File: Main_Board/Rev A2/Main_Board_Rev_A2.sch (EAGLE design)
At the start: 207 parts, among them J1 90814-0208, J12 22-27-2061-06, J15 1241050-5, J2 90814-0206, J3 90814-0208, J4 5504F1-09S-02A-03, J5 22-05-7048-04, J6 22-05-7048-04, J7 22-05-7058-05, J8 22-05-7048-04, K1 G6K-2G-Y, K2 G6K-2G-Y, K3 G6K-2G-Y, K4 G6K-2G-Y, P1 RB1-125BAG1A, SW1 B3FS-1015, SW2 B3FS-1015, T1 MMBT2222AL, U1 LT3686HDDPBF, U10 SN74LVC2G17DBVR, U11 MCP2561-E/SN, U12 TLV313, U2 TPL0401A, U3 SN74LVC3G17DCTR, U4 SN74LVC3G17DCTR, U5 LT3686HDDPBF, U6 LPC1768FBD100, U7 AT24C512C-SSHM-B, U8 SN74LVC3G17DCTR, U9 SN74LVC2G17DBVR, X1 ASE_50, X12 22-05-7028-02, X13 22-05-7028-02, X14 22-05-7038-03, X15 22-05-7038-03, X2 FC-135, X3 ASE-12, X4 MSTBA2, X5 22-05-7028-02, X6 USB3075-30-A, X7 3000, X8 22-05-7028-02

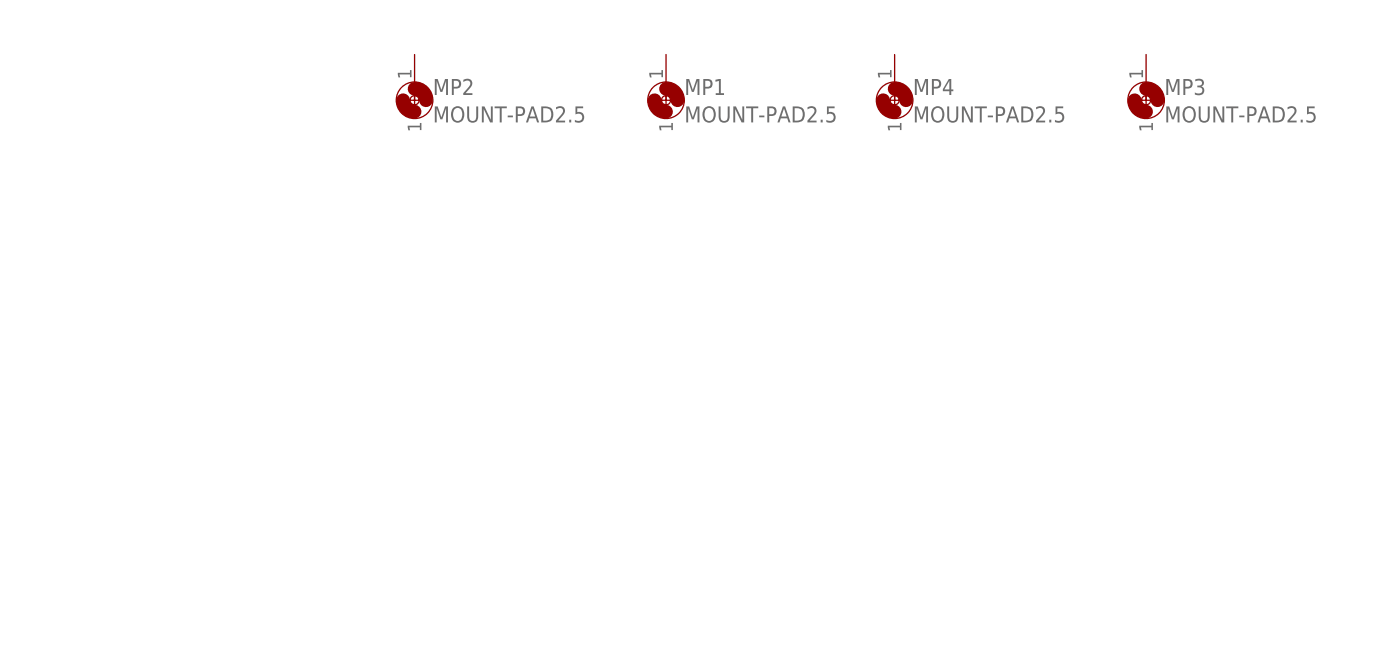
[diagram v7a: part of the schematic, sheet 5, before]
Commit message: Route power and add guard ring on the board
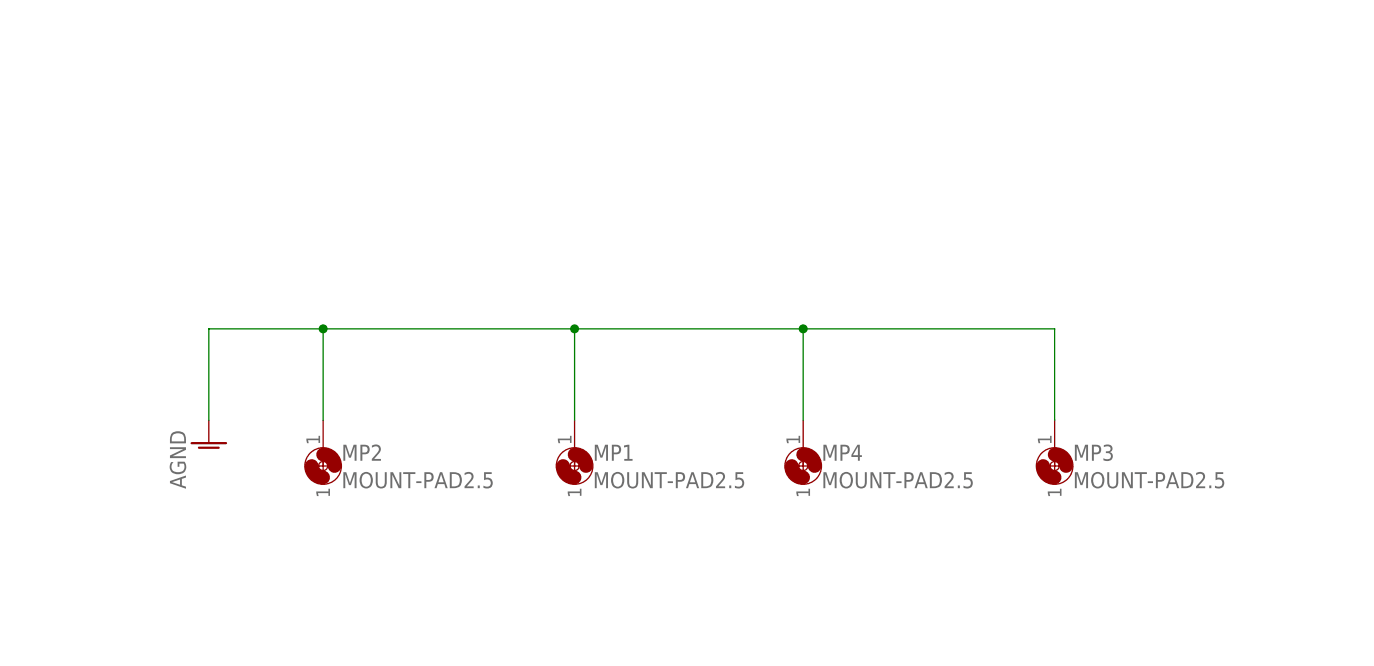
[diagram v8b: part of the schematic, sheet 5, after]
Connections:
- new net AGND: J4S.SHIELD, MP1.1, MP2.1, MP3.1, MP4.1, P1.P$1, X6.S
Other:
- moved on the sheet: MP1, MP2, MP3, MP4
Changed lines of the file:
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@@
 <part name="+3V28" library="supply1" deviceset="+3V3" device=""/>
 <part name="+3V14" library="supply1" deviceset="+3V3" device=""/>
+<part name="AGND1" library="supply1" deviceset="AGND" device=""/>
+<part name="AGND2" library="supply1" deviceset="AGND" device=""/>
+<part name="AGND3" library="supply1" deviceset="AGND" device=""/>
+<part name="AGND4" library="supply1" deviceset="AGND" device=""/>
 </parts>
 <sheets>
@@
 <wire x1="165.1" y1="256.54" x2="165.1" y2="104.14" width="0.1524" layer="97"/>
 <wire x1="165.1" y1="104.14" x2="3.81" y2="104.14" width="0.1524" layer="97"/>
-<wire x1="165.1" y1="104.14" x2="261.62" y2="104.14" width="0.1524" layer="97"/>
-<wire x1="261.62" y1="104.14" x2="383.54" y2="104.14" width="0.1524" layer="97"/>
-<wire x1="261.874" y1="3.81" x2="261.62" y2="104.14" width="0.1524" layer="97"/>
+<wire x1="165.1" y1="104.14" x2="254" y2="104.14" width="0.1524" layer="97"/>
+<wire x1="254" y1="104.14" x2="383.54" y2="104.14" width="0.1524" layer="97"/>
+<wire x1="254.254" y1="3.81" x2="254" y2="104.14" width="0.1524" layer="97"/>
 <wire x1="165.354" y1="3.81" x2="165.1" y2="104.14" width="0.1524" layer="97"/>
 <text x="7.62" y="251.46" size="1.778" layer="97">ETHERNET INPUT</text>
@@
 <instance part="P+15" gate="1" x="111.76" y="93.98"/>
 <instance part="GND19" gate="1" x="88.9" y="66.04"/>
+<instance part="AGND2" gate="VR1" x="109.22" y="45.72"/>
+<instance part="AGND4" gate="VR1" x="45.72" y="154.94"/>
 </instances>
 <busses>
@@
 </segment>
 </net>
+<net name="AGND" class="0">
+<segment>
+<pinref part="J4" gate="S" pin="SHIELD"/>
+<pinref part="AGND2" gate="VR1" pin="AGND"/>
+<wire x1="99.06" y1="55.88" x2="109.22" y2="55.88" width="0.1524" layer="91"/>
+<wire x1="109.22" y1="55.88" x2="109.22" y2="48.26" width="0.1524" layer="91"/>
+</segment>
+<segment>
+<pinref part="P1" gate="G$1" pin="P$1"/>
+<pinref part="AGND4" gate="VR1" pin="AGND"/>
+<wire x1="45.72" y1="165.1" x2="45.72" y2="157.48" width="0.1524" layer="91"/>
+</segment>
+</net>
 </nets>
 </sheet>
@@
 <instance part="TP1" gate="G$1" x="114.3" y="236.22"/>
 <instance part="P+16" gate="1" x="106.68" y="236.22"/>
-<instance part="MP2" gate="1" x="274.32" y="236.22"/>
-<instance part="MP1" gate="1" x="302.26" y="236.22"/>
-<instance part="MP4" gate="1" x="327.66" y="236.22"/>
-<instance part="MP3" gate="1" x="355.6" y="236.22"/>
+<instance part="MP2" gate="1" x="264.16" y="195.58"/>
+<instance part="MP1" gate="1" x="292.1" y="195.58"/>
+<instance part="MP4" gate="1" x="317.5" y="195.58"/>
+<instance part="MP3" gate="1" x="345.44" y="195.58"/>
 <instance part="TP4" gate="G$1" x="106.68" y="195.58" rot="R180"/>
 <instance part="P+17" gate="1" x="25.4" y="177.8"/>
@@
 <attribute name="MPN" x="170.18" y="149.86" size="1.778" layer="96" display="off"/>
 </instance>
+<instance part="AGND1" gate="VR1" x="251.46" y="198.12"/>
 </instances>
 <busses>
@@
 </segment>
 </net>
+<net name="AGND" class="0">
+<segment>
+<pinref part="AGND1" gate="VR1" pin="AGND"/>
+<wire x1="251.46" y1="200.66" x2="251.46" y2="210.82" width="0.1524" layer="91"/>
+<wire x1="251.46" y1="210.82" x2="264.16" y2="210.82" width="0.1524" layer="91"/>
+<pinref part="MP3" gate="1" pin="1"/>
+<wire x1="264.16" y1="210.82" x2="292.1" y2="210.82" width="0.1524" layer="91"/>
+<wire x1="292.1" y1="210.82" x2="317.5" y2="210.82" width="0.1524" layer="91"/>
+<wire x1="317.5" y1="210.82" x2="345.44" y2="210.82" width="0.1524" layer="91"/>
+<wire x1="345.44" y1="210.82" x2="345.44" y2="200.66" width="0.1524" layer="91"/>
+<pinref part="MP4" gate="1" pin="1"/>
+<wire x1="317.5" y1="200.66" x2="317.5" y2="210.82" width="0.1524" layer="91"/>
+<junction x="317.5" y="210.82"/>
+<pinref part="MP1" gate="1" pin="1"/>
+<wire x1="292.1" y1="200.66" x2="292.1" y2="210.82" width="0.1524" layer="91"/>
+<junction x="292.1" y="210.82"/>
+<pinref part="MP2" gate="1" pin="1"/>
+<wire x1="264.16" y1="200.66" x2="264.16" y2="210.82" width="0.1524" layer="91"/>
+<junction x="264.16" y="210.82"/>
+</segment>
+</net>
 </nets>
 </sheet>
@@
 <instance part="+3V324" gate="G$1" x="312.42" y="233.68"/>
 <instance part="GND90" gate="1" x="312.42" y="190.5"/>
+<instance part="AGND3" gate="VR1" x="167.64" y="190.5"/>
 </instances>
 <busses>
@@
 </segment>
 </net>
+<net name="AGND" class="0">
+<segment>
+<pinref part="X6" gate="J$1" pin="S"/>
+<pinref part="AGND3" gate="VR1" pin="AGND"/>
+<wire x1="167.64" y1="200.66" x2="167.64" y2="193.04" width="0.1524" layer="91"/>
+</segment>
+</net>
